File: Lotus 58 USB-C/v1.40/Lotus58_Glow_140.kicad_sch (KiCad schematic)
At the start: 117 parts, among them J3 USB_C_Receptacle_USB2.0, P1 OLED, SW1 Kailh hotswap MX socket, SW10 Kailh hotswap MX socket, SW11 Kailh hotswap MX socket, SW12 Kailh hotswap MX socket, SW13 Kailh hotswap MX socket, SW14 Kailh hotswap MX socket, SW15 Kailh hotswap MX socket, SW16 Kailh hotswap MX socket, SW17 Kailh hotswap MX socket, SW18 Kailh hotswap MX socket, SW19 Kailh hotswap MX socket, SW2 Kailh hotswap MX socket, SW20 Kailh hotswap MX socket, SW21 Kailh hotswap MX socket, SW22 Kailh hotswap MX socket, SW23 Kailh hotswap MX socket, SW24 Kailh hotswap MX socket, SW25 Kailh hotswap MX socket, SW26 Kailh hotswap MX socket, SW27 Kailh hotswap MX socket, SW28 Kailh hotswap MX socket, SW29 Kailh hotswap MX socket, SW3 Kailh hotswap MX socket, SW30 Rotary_Encoder_Switch, SW31 Rotary_Encoder_Switch, SW32 MSK12C02, SW33 MSK12C02, SW4 Kailh hotswap MX socket, SW5 Kailh hotswap MX socket, SW6 Kailh hotswap MX socket, SW7 Kailh hotswap MX socket, SW8 Kailh hotswap MX socket, SW9 Kailh hotswap MX socket, U1 ProMicro, U2 SRV05-4

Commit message: Created STEP files for 3D model
Signed-off-by: TweetyDaBird <markus.knutsson@tweety.se>
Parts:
- added JP1, JP2: LEFT, Keyboard Common:Jumper_min_v2, symbol Jumper:Jumper_2_Open
- JP3, JP4: footprint Keyboard Common:Jumper_Mini -> Keyboard Common:Jumper_min_v2
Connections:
- net GND: now also JP4.1 (A); no longer JP4.2 (B)
- net Hand: now also JP3.2 (B), JP4.2 (B); no longer JP3.1 (A), JP4.1 (A)
- net PWR_GLOW: now also JP1.1 (A)
- net PWR_KEY: now also JP2.1 (A)
- net VCC: now also JP3.1 (A), JP1.2 (B), JP2.2 (B); no longer JP3.2 (B)
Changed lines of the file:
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@@
     (effects (font (size 1.27 1.27)) (justify left bottom))
   )
+  (label "PWR_KEY" (at 241.3 161.29 0) (fields_autoplaced)
+    (effects (font (size 1.27 1.27)) (justify left bottom))
+  )
+  (label "PWR_GLOW" (at 241.3 156.21 0) (fields_autoplaced)
+    (effects (font (size 1.27 1.27)) (justify left bottom))
+  )
   (label "PWR_GLOW" (at 267.97 157.48 0) (fields_autoplaced)
     (effects (font (size 1.27 1.27)) (justify left bottom))
@@
     )
   )
-  (symbol (lib_id "Jumper:Jumper_2_Open") (at 355.6 38.1 0) (unit 1)
+  (symbol (lib_id "Jumper:Jumper_2_Open") (at 355.6 38.1 0) (mirror y) (unit 1)
     (in_bom yes) (on_board yes) (dnp no)
     (property "Reference" "JP3" (at 355.6 39.37 0)
@@
       (effects (font (size 1.27 1.27)) hide)
     )
-    (property "Footprint" "Keyboard Common:Jumper_Mini" (at 355.6 38.1 0)
+    (property "Footprint" "Keyboard Common:Jumper_min_v2" (at 355.6 38.1 0)
       (effects (font (size 1.27 1.27)) hide)
     )
@@
     )
   )
-  (symbol (lib_id "Jumper:Jumper_2_Open") (at 355.6 41.91 0) (unit 1)
+  (symbol (lib_id "Jumper:Jumper_2_Open") (at 355.6 41.91 0) (mirror y) (unit 1)
     (in_bom yes) (on_board yes) (dnp no)
     (property "Reference" "JP4" (at 355.6 43.18 0)
@@
       (effects (font (size 1.27 1.27)) hide)
     )
-    (property "Footprint" "Keyboard Common:Jumper_Mini" (at 355.6 41.91 0)
+    (property "Footprint" "Keyboard Common:Jumper_min_v2" (at 355.6 41.91 0)
       (effects (font (size 1.27 1.27)) hide)
     )
@@
     )
   )
+  (symbol (lib_id "Jumper:Jumper_2_Open") (at 236.22 156.21 0) (mirror y) (unit 1)
+    (in_bom yes) (on_board yes) (dnp no)
+    (property "Reference" "JP1" (at 236.22 157.48 0)
+      (effects (font (size 1.27 1.27)))
+    )
+    (property "Value" "LEFT" (at 236.22 153.8224 0)
+      (effects (font (size 1.27 1.27)) hide)
+    )
+    (property "Footprint" "Keyboard Common:Jumper_min_v2" (at 236.22 156.21 0)
+      (effects (font (size 1.27 1.27)) hide)
+    )
+    (property "Datasheet" "~" (at 236.22 156.21 0)
+      (effects (font (size 1.27 1.27)) hide)
+    )
+    (pin "1")
+    (pin "2")
+    (instances
+      (project "Lotus58_Glow_140"
+        (path "/033c564d-3d11-4dc7-8633-0c6732489a73"
+          (reference "JP1") (unit 1)
+        )
+      )
+    )
+  )
+  (symbol (lib_id "power:VCC") (at 231.14 161.29 90) (unit 1)
+    (in_bom yes) (on_board yes) (dnp no)
+    (property "Reference" "#PWR021" (at 234.95 161.29 0)
+      (effects (font (size 1.27 1.27)) hide)
+    )
+    (property "Value" "VCC" (at 226.7458 160.8582 0)
+      (effects (font (size 1.27 1.27)))
+    )
+    (property "Footprint" "" (at 231.14 161.29 0)
+      (effects (font (size 1.27 1.27)) hide)
+    )
+    (property "Datasheet" "" (at 231.14 161.29 0)
+      (effects (font (size 1.27 1.27)) hide)
+    )
+    (pin "1")
+    (instances
+      (project "Lotus58_Glow_140"
+        (path "/033c564d-3d11-4dc7-8633-0c6732489a73"
+          (reference "#PWR021") (unit 1)
+        )
+      )
+    )
+  )
   (symbol (lib_id "Logotypes:QMK_Logo") (at 384.81 227.33 0) (unit 1)
     (in_bom no) (on_board yes) (dnp no) (fields_autoplaced)
@@
     )
   )
+  (symbol (lib_id "Jumper:Jumper_2_Open") (at 236.22 161.29 0) (mirror y) (unit 1)
+    (in_bom yes) (on_board yes) (dnp no)
+    (property "Reference" "JP2" (at 236.22 162.56 0)
+      (effects (font (size 1.27 1.27)))
+    )
+    (property "Value" "LEFT" (at 236.22 158.9024 0)
+      (effects (font (size 1.27 1.27)) hide)
+    )
+    (property "Footprint" "Keyboard Common:Jumper_min_v2" (at 236.22 161.29 0)
+      (effects (font (size 1.27 1.27)) hide)
+    )
+    (property "Datasheet" "~" (at 236.22 161.29 0)
+      (effects (font (size 1.27 1.27)) hide)
+    )
+    (pin "1")
+    (pin "2")
+    (instances
+      (project "Lotus58_Glow_140"
+        (path "/033c564d-3d11-4dc7-8633-0c6732489a73"
+          (reference "JP2") (unit 1)
+        )
+      )
+    )
+  )
   (symbol (lib_id "Keyboard Common:SK6812MINI-E") (at 276.86 213.36 0) (unit 1)
     (in_bom yes) (on_board yes) (dnp no)
@@
         )
       )
+    )
+  )
+  (symbol (lib_id "power:VCC") (at 231.14 156.21 90) (unit 1)
+    (in_bom yes) (on_board yes) (dnp no)
+    (property "Reference" "#PWR019" (at 234.95 156.21 0)
+      (effects (font (size 1.27 1.27)) hide)
+    )
+    (property "Value" "VCC" (at 226.7458 155.7782 0)
+      (effects (font (size 1.27 1.27)))
+    )
+    (property "Footprint" "" (at 231.14 156.21 0)
+      (effects (font (size 1.27 1.27)) hide)
+    )
+    (property "Datasheet" "" (at 231.14 156.21 0)
+      (effects (font (size 1.27 1.27)) hide)
+    )
+    (pin "1")
+    (instances
+      (project "Lotus58_Glow_140"
+        (path "/033c564d-3d11-4dc7-8633-0c6732489a73"
+          (reference "#PWR019") (unit 1)
+        )
+      )

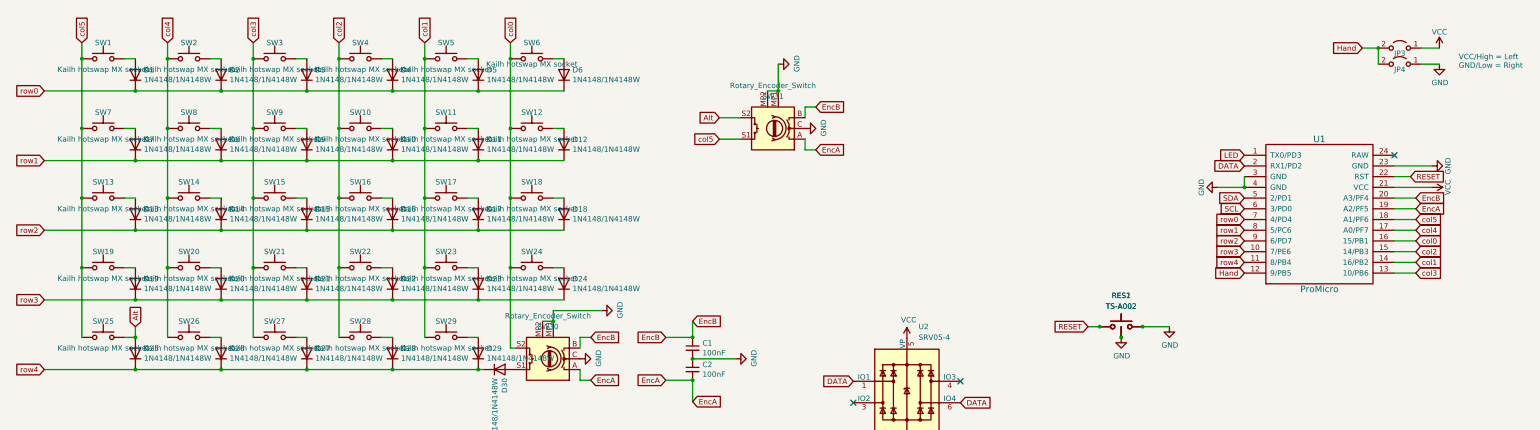
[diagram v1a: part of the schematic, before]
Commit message: Initial changes for kailh choc V1 hostswaps
* Changed footprint for switches to kailh choc V1 hotswaps
* Change per-key and underglow LED positions
* Rerouted all tracks for LEDS and switches
* Removed encoder near thumb cluster
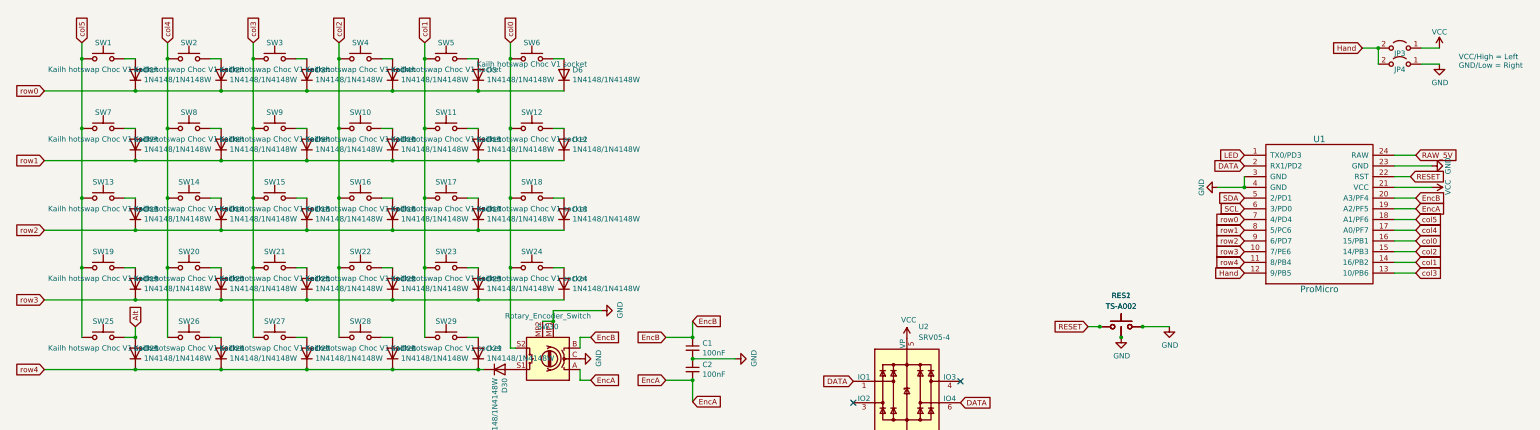
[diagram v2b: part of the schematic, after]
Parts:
- removed SW31: Rotary_Encoder_Switch, Keyboard Encoders:Encoder_Alps_EC11E_Offset_pad, symbol Keyboard Switches:Rotary_Encoder_Click
- SW1, SW10, SW11, SW12, SW13, SW14, SW15, SW16, SW17, SW18, SW19, SW2, SW20, SW21, SW22, SW23, SW24, SW25, SW26, SW27, SW28, SW29, SW3, SW4, SW5, SW6, SW7, SW8, SW9: value Kailh hotswap MX socket -> Kailh hotswap Choc V1 socket; footprint Keyboard Switches:SW_MX_HotSwap_Reversible -> Spencer-Custom:SW_Kailh_Choc_V1_HotSwap_Reversible
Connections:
- net RAW_5V: now reaches U1.24 (RAW)
- no-connect marks 11 -> 10

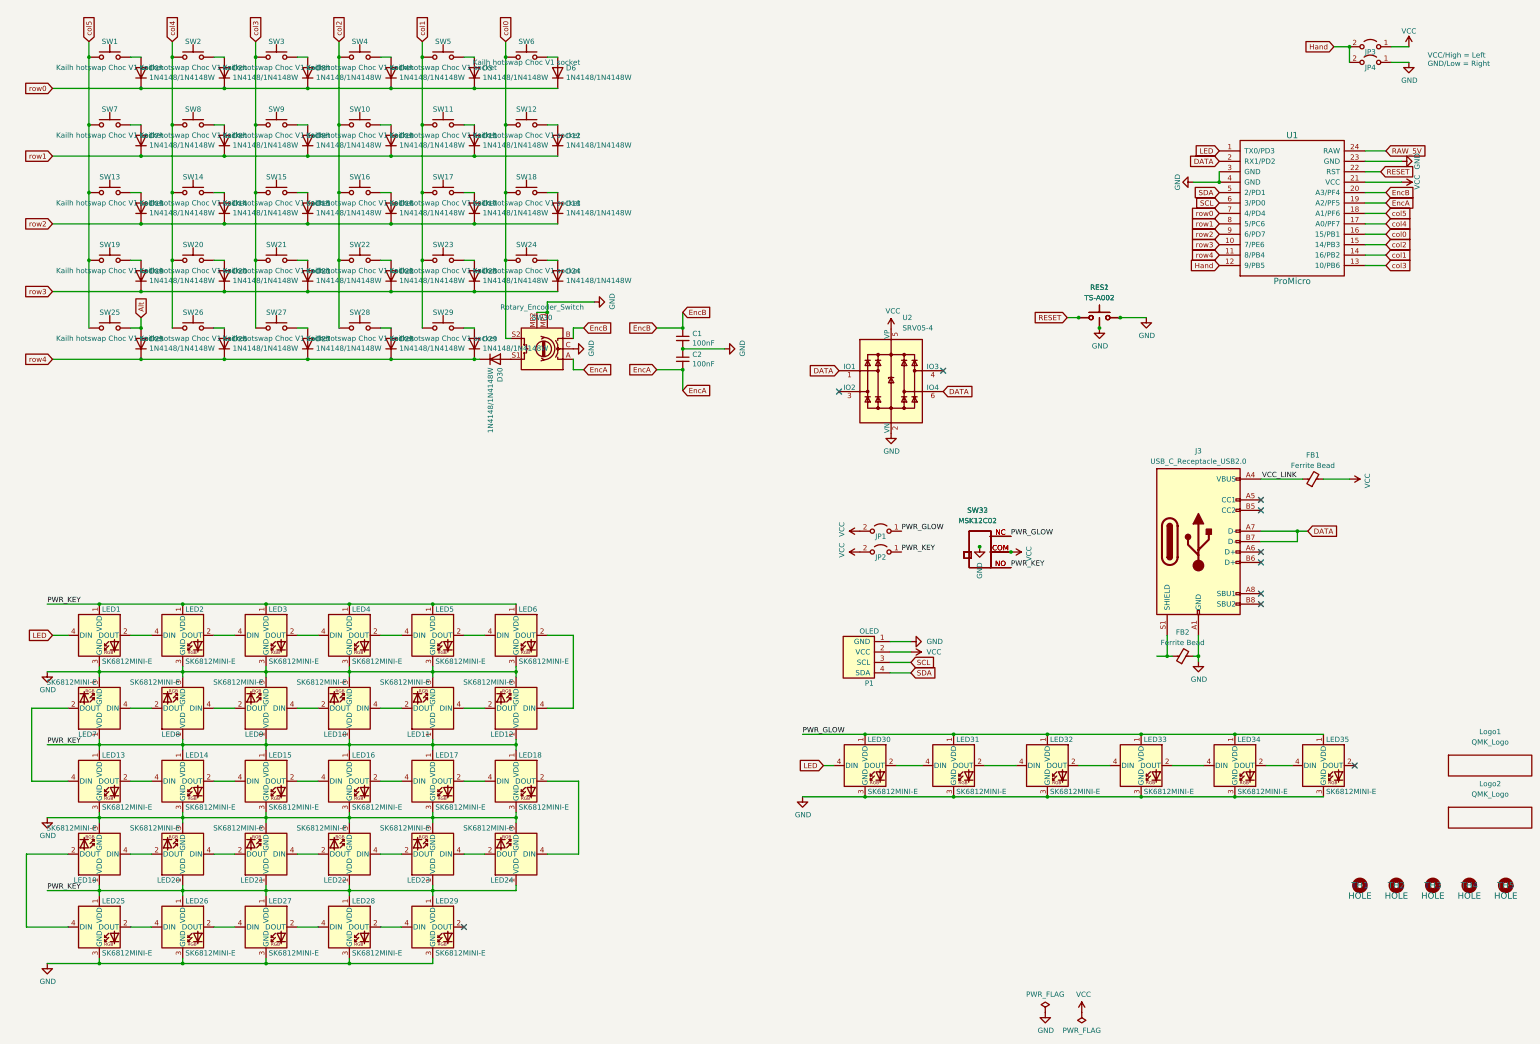
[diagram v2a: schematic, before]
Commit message: Add voltage translator for LEDs with RP2040
* Added voltage translator
  - Routed USB Raw 5V from controller board to LED translator for use by
    LEDs
* Rerouted power link between boards to use USB Raw 5V instead of
  controller VCC
* Added additional backside placement for components
* Fixed schematic parity with pcb
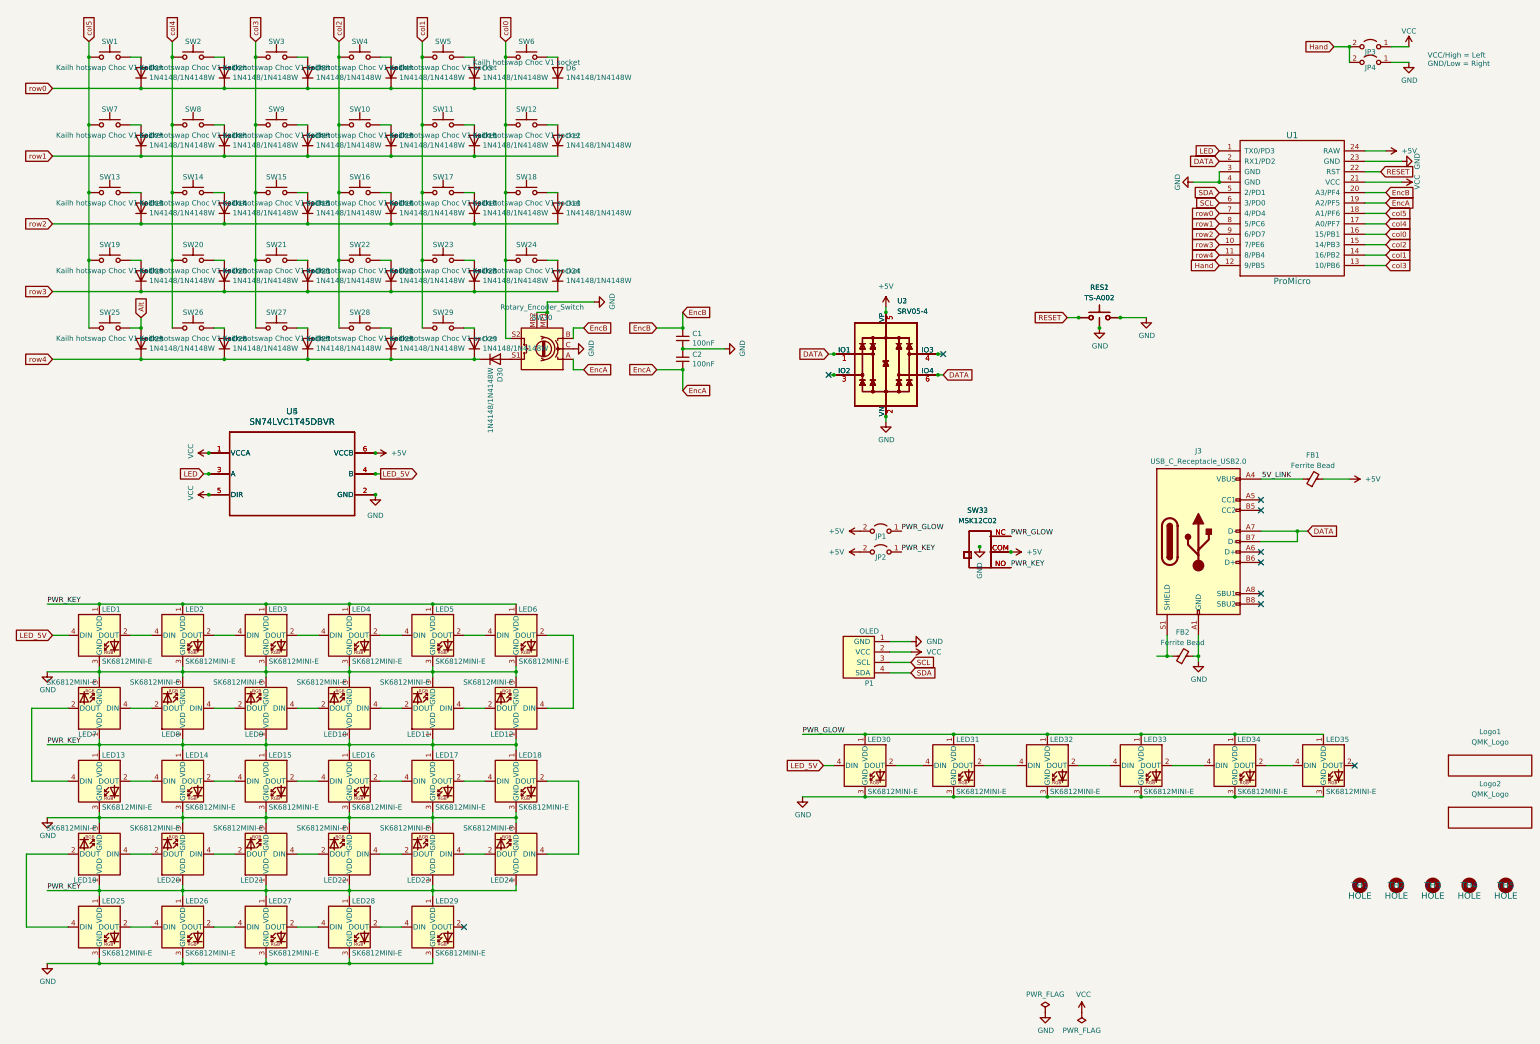
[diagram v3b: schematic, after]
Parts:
- added U3: SRV05-4, Package_TO_SOT_SMD:SOT-23-6, symbol LCSC Parts:SRV05-4
- added U4, U5: SN74LVC1T45DBVR, Spencer-Custom:DBV0006A_N, symbol Spencer-Custom:SN74LVC1T45DBVR
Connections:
- net DATA: now also U3.1 (IO1), U3.6 (IO4)
- net GND: now also U3.2 (VN), U4.2 (GND), U5.2 (GND)
- net LED: now also U4.3 (A), U5.3 (A); no longer LED1.4 (DIN), LED30.4 (DIN)
- net VCC: now also U4.1 (VCCA), U4.5 (DIR), U5.1 (VCCA), U5.5 (DIR); no longer FB1.2, JP1.2 (B), JP2.2 (B), SW32.COM, SW33.COM, U2.5 (VP)
- net at U2.3 (IO2): now also U3.3 (IO2)
- net at U2.4 (IO3): now also U3.4 (IO3)
- net RAW_5V renamed +5V
- net +5V: now also FB1.2, JP1.2 (B), JP2.2 (B), SW32.COM, SW33.COM, U2.5 (VP), U3.5 (VP), U4.6 (VCCB), U5.6 (VCCB)
- net VCC_LINK renamed 5V_LINK
- new net LED_5V: LED1.4 (DIN), LED30.4 (DIN), U4.4 (B), U5.4 (B)
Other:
- moved on the sheet: U2

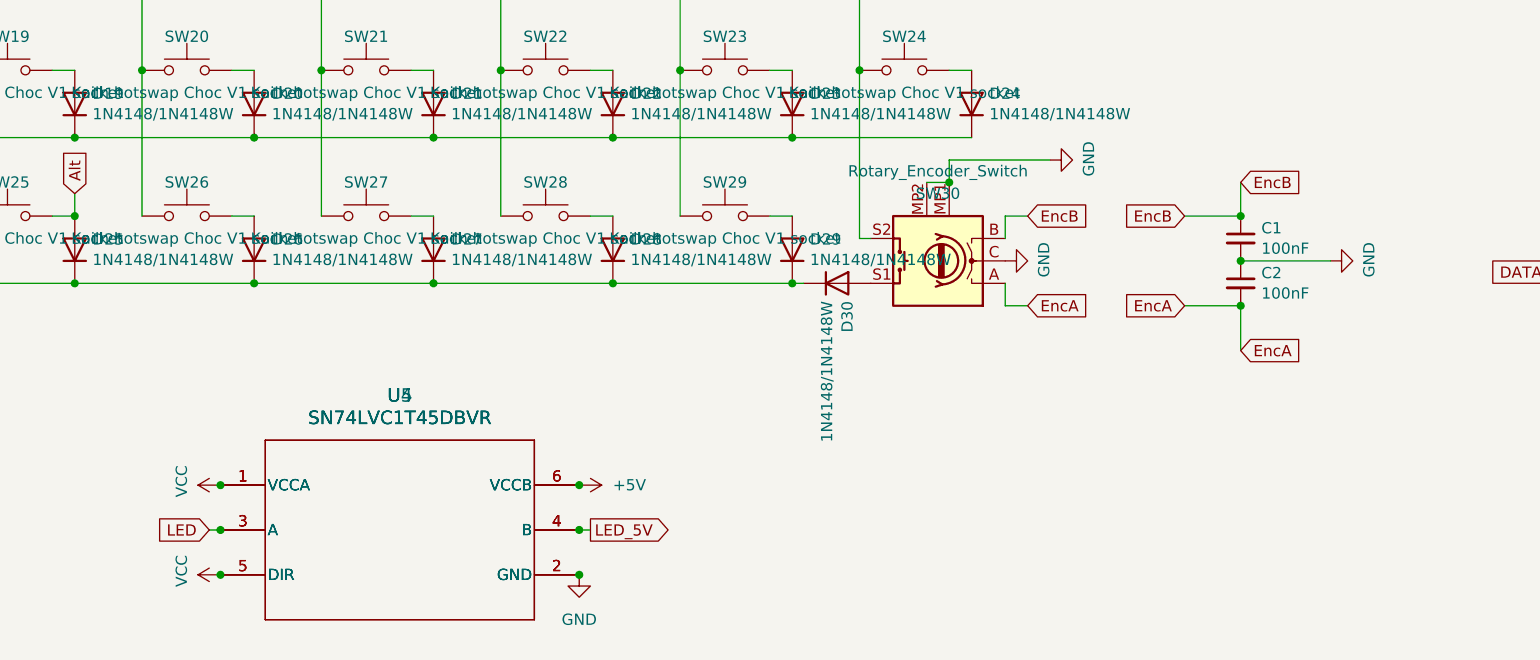
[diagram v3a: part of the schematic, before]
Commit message: Added decoupling capacitors for level shifter
* Also changed encoder decoupling capacitors to SMD components
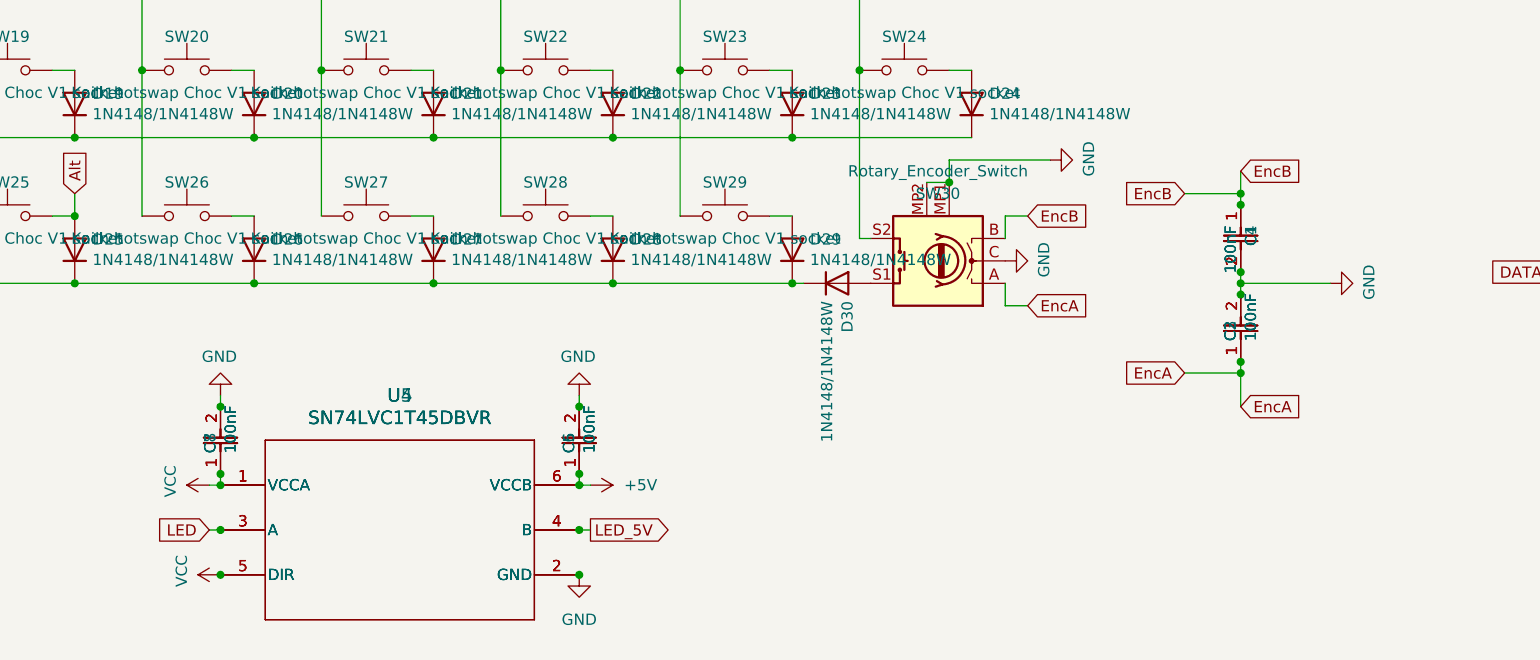
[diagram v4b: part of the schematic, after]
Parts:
- added C3, C4, C5, C6, C7, C8: 100nF, Spencer-Custom:CAP_CL05_SAM, symbol Spencer-Custom:CL05B104KP5NNNC
- C1, C2: footprint Keyboard Common:RESISTOR_Reversible -> Spencer-Custom:CAP_CL05_SAM; symbol Device:C_Small -> Spencer-Custom:CL05B104KP5NNNC
- J3: footprint LCSC_Library:Molex-216990_GCT-USB45xx_HRO-TYPE-C-31-M-13x-PiMicro -> Keyboard Common:Molex-216990_GCT-USB45xx_HRO-TYPE-C-31-M-13x-PiMicro
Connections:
- net +5V: now also C5.1, C6.1
- net EncA: now also C2.1, C3.1; no longer C2.2
- net EncB: now also C4.1
- net GND: now also C2.2, C3.2, C4.2, C5.2, C6.2, C7.2, C8.2; no longer C2.1
- net VCC: now also C7.1, C8.1
